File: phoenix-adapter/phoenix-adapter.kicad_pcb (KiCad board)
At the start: 2 copper layers, 16.2 x 20 mm, 2 parts, among them CON101 RCJ-2223

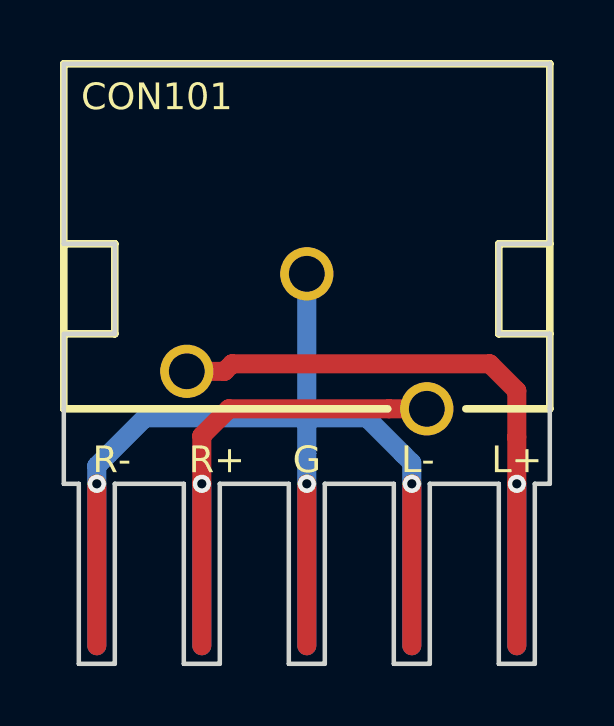
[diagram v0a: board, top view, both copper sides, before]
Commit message: Modified with basic solder jumper to ground the negative pins for use as an unbalanced input
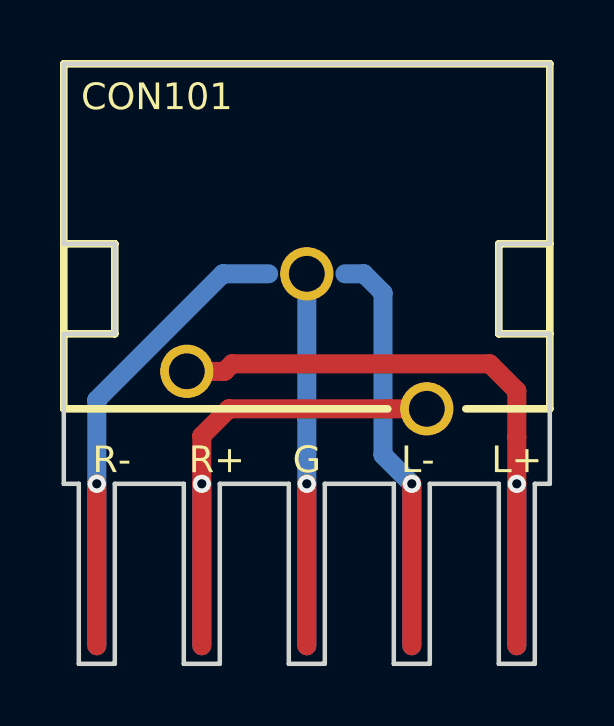
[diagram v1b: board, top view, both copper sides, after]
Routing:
- net GND: track 52.5 -> 58.0 mm
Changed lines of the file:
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@@
-(kicad_pcb (version 4) (host pcbnew 4.0.7-e2-6376~58~ubuntu16.04.1)
+(kicad_pcb (version 4) (host pcbnew 4.0.7)
   (general
     (links 0)
     (no_connects 0)
-    (area 131.295199 104.0983 148.104801 127.375001)
+    (area 131.524999 107.224999 147.875001 127.375001)
     (thickness 1.6)
-    (drawings 40)
-    (tracks 36)
+    (drawings 43)
+    (tracks 35)
     (zones 0)
     (modules 2)
@@
     (38 B.Mask user)
     (39 F.Mask user)
-    (40 Dwgs.User user)
+    (40 Dwgs.User user hide)
     (41 Cmts.User user)
     (42 Eco1.User user)
@@
     (44 Edge.Cuts user)
     (45 Margin user)
-    (46 B.CrtYd user)
-    (47 F.CrtYd user)
-    (48 B.Fab user)
-    (49 F.Fab user)
+    (46 B.CrtYd user hide)
+    (47 F.CrtYd user hide)
+    (48 B.Fab user hide)
+    (49 F.Fab user hide)
   )
   (setup
@@
     (pad_to_mask_clearance 0.2)
     (aux_axis_origin 0 0)
-    (grid_origin 139.7 114.3)
-    (visible_elements FFFFFF7F)
+    (grid_origin 139.065 114.3)
+    (visible_elements 7FFFFFFF)
     (pcbplotparams
       (layerselection 0x010f0_80000001)
@@
       (drillshape 0)
       (scaleselection 1)
-      (outputdirectory gerbers/0.1/))
+      (outputdirectory gerbers/0.1.1/))
   )
   (net 0 "")
@@
       (xy 3.762644 0.861017)) (layer B.SilkS) (width 0.01))
   )
-  (gr_text db-electronics.ca (at 141.4 111.9) (layer B.SilkS)
+  (dimension 16.51 (width 0.3) (layer B.Mask)
+    (gr_text "16.510 mm" (at 139.7 95.805) (layer B.Mask)
+      (effects (font (size 1.5 1.5) (thickness 0.3)))
+    )
+    (feature1 (pts (xy 147.955 101.6) (xy 147.955 94.455)))
+    (feature2 (pts (xy 131.445 101.6) (xy 131.445 94.455)))
+    (crossbar (pts (xy 131.445 97.155) (xy 147.955 97.155)))
+    (arrow1a (pts (xy 147.955 97.155) (xy 146.828496 97.741421)))
+    (arrow1b (pts (xy 147.955 97.155) (xy 146.828496 96.568579)))
+    (arrow2a (pts (xy 131.445 97.155) (xy 132.571504 97.741421)))
+    (arrow2b (pts (xy 131.445 97.155) (xy 132.571504 96.568579)))
+  )
+  (dimension 19.685 (width 0.3) (layer B.Mask)
+    (gr_text "19.685 mm" (at 124.38 117.1575 270) (layer B.Mask)
+      (effects (font (size 1.5 1.5) (thickness 0.3)))
+    )
+    (feature1 (pts (xy 131.445 127) (xy 123.03 127)))
+    (feature2 (pts (xy 131.445 107.315) (xy 123.03 107.315)))
+    (crossbar (pts (xy 125.73 107.315) (xy 125.73 127)))
+    (arrow1a (pts (xy 125.73 127) (xy 125.143579 125.873496)))
+    (arrow1b (pts (xy 125.73 127) (xy 126.316421 125.873496)))
+    (arrow2a (pts (xy 125.73 107.315) (xy 125.143579 108.441504)))
+    (arrow2b (pts (xy 125.73 107.315) (xy 126.316421 108.441504)))
+  )
+  (gr_line (start 138.43 114.3) (end 140.97 114.3) (layer B.Mask) (width 1))
+  (gr_text db-electronics.ca (at 141.4 111.76) (layer B.SilkS)
     (effects (font (size 0.889 0.889) (thickness 0.2032)) (justify mirror))
   )
@@
   (gr_line (start 131.6 113.3) (end 133.3 113.3) (layer Edge.Cuts) (width 0.15))
   (gr_line (start 131.6 107.3) (end 131.6 113.3) (layer Edge.Cuts) (width 0.15))
+  (segment (start 141.605 114.3) (end 140.97 114.3) (width 0.635) (layer B.Cu) (net 1))
+  (segment (start 142.24 114.935) (end 141.605 114.3) (width 0.635) (layer B.Cu) (net 1))
+  (segment (start 142.24 120.34) (end 142.24 114.935) (width 0.635) (layer B.Cu) (net 1))
+  (segment (start 136.901234 114.3) (end 138.43 114.3) (width 0.635) (layer B.Cu) (net 1))
+  (segment (start 143.2 121.3) (end 142.24 120.34) (width 0.635) (layer B.Cu) (net 1))
+  (segment (start 136.901234 114.3) (end 132.7 118.501234) (width 0.635) (layer B.Cu) (net 1))
+  (segment (start 132.7 118.501234) (end 132.7 121.3) (width 0.635) (layer B.Cu) (net 1))
   (segment (start 143.2 121.3) (end 143.2 126.7) (width 0.635) (layer F.Cu) (net 1))
   (segment (start 143.2 121.3) (end 143.2 126.7) (width 0.635) (layer B.Cu) (net 1))
-  (segment (start 143.2 120.6) (end 143.2 121.3) (width 0.635) (layer B.Cu) (net 1))
   (via (at 143.2 121.3) (size 0.6096) (drill 0.3048) (layers F.Cu B.Cu) (net 1))
   (segment (start 139.7 121.3) (end 139.7 126.7) (width 0.635) (layer F.Cu) (net 1))
@@
   (segment (start 132.7 121.3) (end 132.7 126.7) (width 0.635) (layer F.Cu) (net 1))
   (segment (start 132.7 121.3) (end 132.7 126.7) (width 0.635) (layer B.Cu) (net 1))
-  (segment (start 132.7 120.7) (end 132.7 121.3) (width 0.635) (layer B.Cu) (net 1))
   (via (at 132.7 121.3) (size 0.6096) (drill 0.3048) (layers F.Cu B.Cu) (net 1))
-  (segment (start 142.9 120.3) (end 141.7 119.1) (width 0.635) (layer B.Cu) (net 1))
-  (segment (start 141.7 119.1) (end 139.7 119.1) (width 0.635) (layer B.Cu) (net 1))
-  (segment (start 139.7 114.3) (end 139.7 119.1) (width 0.635) (layer B.Cu) (net 1))
+  (segment (start 139.7 114.3) (end 139.7 119.1) (width 0.635) (layer B.Cu) (net 1) (status 10))
   (segment (start 139.7 119.1) (end 139.7 120.3) (width 0.635) (layer B.Cu) (net 1))
-  (segment (start 133.1 120.3) (end 134.3 119.1) (width 0.635) (layer B.Cu) (net 1))
-  (segment (start 134.3 119.1) (end 139.7 119.1) (width 0.635) (layer B.Cu) (net 1))
-  (segment (start 133.1 120.3) (end 132.7 120.7) (width 0.635) (layer B.Cu) (net 1))
-  (segment (start 142.9 120.3) (end 143.2 120.6) (width 0.635) (layer B.Cu) (net 1))
-  (segment (start 135.7 117.55) (end 136.957235 117.55) (width 0.635) (layer F.Cu) (net 2))
+  (segment (start 135.7 117.55) (end 136.957235 117.55) (width 0.635) (layer F.Cu) (net 2) (status 10))
   (segment (start 136.957235 117.55) (end 137.207235 117.3) (width 0.635) (layer F.Cu) (net 2))
   (segment (start 146.7 118.2) (end 146.7 119.751234) (width 0.635) (layer F.Cu) (net 2))
@@
   (segment (start 137.1 118.8) (end 136.2 119.7) (width 0.635) (layer F.Cu) (net 3))
   (segment (start 142.442765 118.8) (end 137.1 118.8) (width 0.635) (layer F.Cu) (net 3))
-  (segment (start 143.7 118.8) (end 142.442765 118.8) (width 0.635) (layer F.Cu) (net 3))
+  (segment (start 143.7 118.8) (end 142.442765 118.8) (width 0.635) (layer F.Cu) (net 3) (status 10))
   (zone (net 0) (net_name "") (layer F.Mask) (hatch edge 0.508)
     (connect_pads (clearance 0.508))
